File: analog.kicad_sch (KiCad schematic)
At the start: 38 parts, among them Q3 BSS138, U1 TL494, U4 NE5532, U5 INA180A2

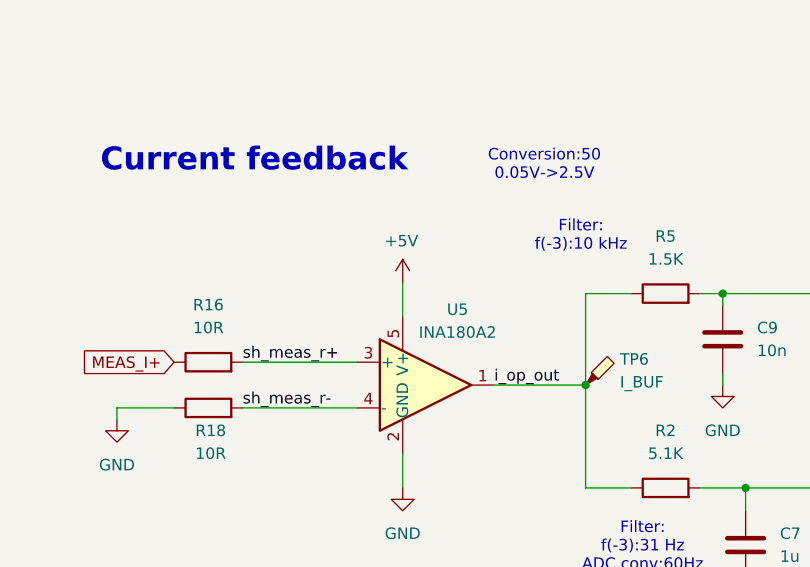
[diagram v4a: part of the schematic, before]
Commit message: approximate location of the components at the PCB
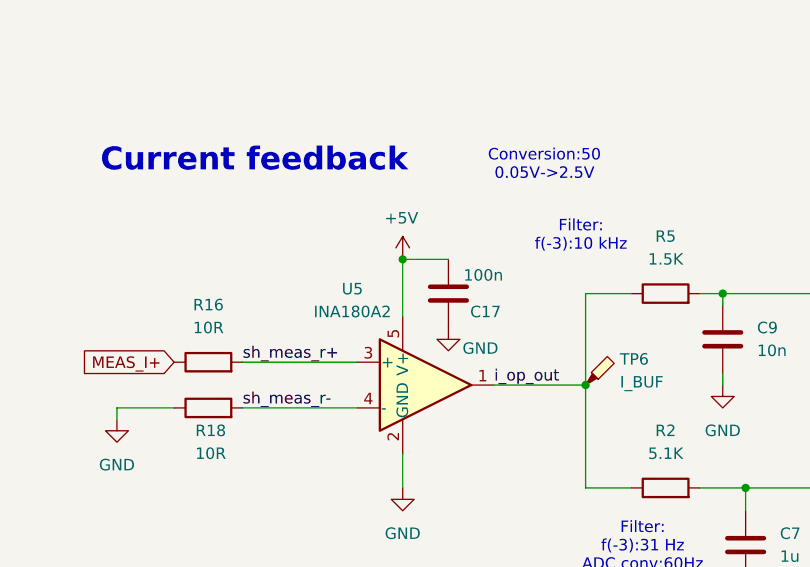
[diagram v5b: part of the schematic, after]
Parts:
- added C17: 100n, Capacitor_SMD:C_0805_2012Metric_Pad1.18x1.45mm_HandSolder, symbol Device:C
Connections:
- net +5V: now also C17.2
- net GND: now also C17.1
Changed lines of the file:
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@@
 	)
 	(junction
+		(at 62.23 133.35)
+		(diameter 0)
+		(color 0 0 0 0)
+	)
+	(junction
 		(at 250.19 97.79)
 		(diameter 0)
@@
 	(wire
 		(pts
+			(xy 62.23 133.35) (xy 67.31 133.35)
+		)
+		(stroke
+			(width 0)
+			(type default)
+		)
+	)
+	(wire
+		(pts
 			(xy 256.54 97.79) (xy 259.08 97.79)
 		)
@@
 	(wire
 		(pts
+			(xy 62.23 133.35) (xy 62.23 139.7)
+		)
+		(stroke
+			(width 0)
+			(type default)
+		)
+	)
+	(wire
+		(pts
 			(xy 107.95 38.1) (xy 105.41 38.1)
 		)
@@
 	(wire
 		(pts
-			(xy 62.23 135.89) (xy 62.23 139.7)
-		)
-		(stroke
-			(width 0)
-			(type default)
-		)
-	)
-	(wire
-		(pts
 			(xy 250.19 97.79) (xy 250.19 102.87)
 		)
@@
 	(symbol
 		(lib_id "power:GND")
+		(at 67.31 140.97 0)
+		(unit 1)
+		(exclude_from_sim no)
+		(in_bom yes)
+		(on_board yes)
+		(dnp no)
+		(property "Reference" "#PWR051"
+			(at 67.31 147.32 0)
+			(effects
+				(font
+					(size 1.27 1.27)
+				)
+				(hide yes)
+			)
+		)
+		(property "Value" "GND"
+			(at 70.866 143.256 0)
+			(effects
+				(font
+					(size 1.27 1.27)
+				)
+			)
+		)
+		(property "Footprint" ""
+			(at 67.31 140.97 0)
+			(effects
+				(font
+					(size 1.27 1.27)
+				)
+				(hide yes)
+			)
+		)
+		(property "Datasheet" ""
+			(at 67.31 140.97 0)
+			(effects
+				(font
+					(size 1.27 1.27)
+				)
+				(hide yes)
+			)
+		)
+		(property "Description" "Power symbol creates a global label with name \"GND\" , ground"
+			(at 67.31 140.97 0)
+			(effects
+				(font
+					(size 1.27 1.27)
+				)
+				(hide yes)
+			)
+		)
+		(pin "1"
+		)
+		(instances
+			(project "RPS_ATX"
+				(path "/485c2fed-5176-4ba8-b79d-ac7eddb44491/75639b50-c04a-47dd-b6e6-c8da699a633c"
+					(reference "#PWR051")
+					(unit 1)
+				)
+			)
+		)
+	)
+	(symbol
+		(lib_id "power:GND")
 		(at 92.71 35.56 0)
 		(unit 1)
@@
 		(dnp no)
 		(property "Reference" "U5"
-			(at 68.326 138.938 0)
+			(at 56.642 136.652 0)
 			(effects
 				(font
@@
 		)
 		(property "Value" "INA180A2"
-			(at 68.326 141.478 0)
+			(at 56.642 139.192 0)
 			(effects
 				(font
@@
 	(symbol
 		(lib_id "power:+2V5")
-		(at 62.23 135.89 0)
+		(at 62.23 133.35 0)
 		(unit 1)
 		(exclude_from_sim no)
@@
 		(dnp no)
 		(property "Reference" "#PWR01"
-			(at 62.23 139.7 0)
+			(at 62.23 137.16 0)
 			(effects
 				(font
@@
 		)
 		(property "Value" "+5V"
-			(at 60.198 131.318 0)
+			(at 60.198 128.778 0)
 			(effects
 				(font
@@
 		)
 		(property "Footprint" ""
-			(at 62.23 135.89 0)
+			(at 62.23 133.35 0)
 			(effects
 				(font
@@
 		)
 		(property "Datasheet" ""
-			(at 62.23 135.89 0)
+			(at 62.23 133.35 0)
 			(effects
 				(font
@@
 		)
 		(property "Description" "Power symbol creates a global label with name \"+2V5\""
-			(at 62.23 135.89 0)
+			(at 62.23 133.35 0)
 			(effects
 				(font
@@
 					(unit 1)
 				)
+			)
+		)
+	)
+	(symbol
+		(lib_id "Device:C")
+		(at 67.31 137.16 180)
+		(unit 1)
+		(exclude_from_sim no)
+		(in_bom yes)
+		(on_board yes)
+		(dnp no)
+		(property "Reference" "C17"
+			(at 73.152 139.192 0)
+			(effects
+				(font
+					(size 1.27 1.27)
+				)
+				(justify left)
+			)
+		)
+		(property "Value" "100n"
+			(at 73.406 135.128 0)
+			(effects
+				(font
+					(size 1.27 1.27)
+				)
+				(justify left)
+			)
+		)
+		(property "Footprint" "Capacitor_SMD:C_0805_2012Metric_Pad1.18x1.45mm_HandSolder"
+			(at 66.3448 133.35 0)
+			(effects
+				(font
+					(size 1.27 1.27)
+				)
+				(hide yes)
+			)
+		)
+		(property "Datasheet" "~"
+			(at 67.31 137.16 0)
+			(effects
+				(font
+					(size 1.27 1.27)
+				)
+				(hide yes)
+			)
+		)
+		(property "Description" "Unpolarized capacitor"
+			(at 67.31 137.16 0)
+			(effects
+				(font
+					(size 1.27 1.27)
+				)
+				(hide yes)
+			)
+		)
+		(pin "2"
+		)
+		(pin "1"
+		)
+		(instances
+			(project "RPS_ATX"
+				(path "/485c2fed-5176-4ba8-b79d-ac7eddb44491/75639b50-c04a-47dd-b6e6-c8da699a633c"
+					(reference "C17")
+					(unit 1)
+				)

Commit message: final location of the power,analog sections
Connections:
- net I_2IN-: now also R25.2; no longer C9.1, R5.2
- net U_1IN-: now also R24.2; no longer C18.1, R14.2
- net I_2IN+: now reaches U1.16 (2IN+)
- net I_2IN+: now also C9.1, R5.2; no longer R25.2
- net U_1IN+: now reaches U1.1 (1IN+)
- net U_1IN+: now also C18.1, R14.2; no longer R24.2
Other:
- moved on the sheet: C19, C3, C34, C35, C4, C5, Q3, R1, R13, R24, R25, R3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

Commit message: added display and encoders signal lines, hints
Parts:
- removed U4: NE5532, Package_SO:SOIC-8_3.9x4.9mm_P1.27mm, symbol Amplifier_Operational:NE5532
- added C13, C14: 100n, Capacitor_SMD:C_0805_2012Metric_Pad1.18x1.45mm_HandSolder, symbol Device:C
- added U9: OP07, Package_SO:SOIC-8_3.9x4.9mm_P1.27mm, symbol Amplifier_Operational:OP07
- RV1: value 100K -> U_RV
- RV2: value 100K -> I_RV
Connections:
- net +15V: now also C14.1, U9.7 (V+)
- net GND: now also C13.2, C14.2
- net at R14.1, R15.2, R17.1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: now also U9.6
- net at R15.1, R6.2: now also U9.2 (-)
- net at R4.2, R8.1: now also U9.3 (+)
- new net -5V: C13.1, U9.4 (V-)
- no-connect marks 0 -> 2
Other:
- moved on the sheet: R15, R8

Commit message: added fan control and ds18b20 to the schematic
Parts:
- removed Q3: BSS138, Package_TO_SOT_SMD:SOT-23, symbol Transistor_FET:BSS138
- added Q2: AO3400A, Package_TO_SOT_SMD:SOT-23, symbol Transistor_FET:AO3400A
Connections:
- net DTC: now also Q2.3 (D)
- net GND: now also Q2.2 (S)
- net at C5.1, R1.2: now also Q2.1 (G)
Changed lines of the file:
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@@
+	)
+	(symbol
+		(lib_id "Transistor_FET:AO3400A")
+		(at 250.19 142.24 0)
+		(unit 1)
+		(exclude_from_sim no)
+		(in_bom yes)
+		(on_board yes)
+		(dnp no)
+		(fields_autoplaced yes)
+		(property "Reference" "Q2"
+			(at 256.54 140.9699 0)
+			(effects
+				(font
+					(size 1.27 1.27)
+				)
+				(justify left)
+			)
+		)
+		(property "Value" "AO3400A"
+			(at 256.54 143.5099 0)
+			(effects
+				(font
+					(size 1.27 1.27)
+				)
+				(justify left)
+			)
+		)
+		(property "Footprint" "Package_TO_SOT_SMD:SOT-23"
+			(at 255.27 144.145 0)
+			(effects
+				(font
+					(size 1.27 1.27)
+					(italic yes)
+				)
+				(justify left)
+				(hide yes)
+			)
+		)
+		(property "Datasheet" "http://www.aosmd.com/pdfs/datasheet/AO3400A.pdf"
+			(at 255.27 146.05 0)
+			(effects
+				(font
+					(size 1.27 1.27)
+				)
+				(justify left)
+				(hide yes)
+			)
+		)
+		(property "Description" "30V Vds, 5.7A Id, N-Channel MOSFET, SOT-23"
+			(at 250.19 142.24 0)
+			(effects
+				(font
+					(size 1.27 1.27)
+				)
+				(hide yes)
+			)
+		)
+		(pin "3"
+		)
+		(pin "2"
+		)
+		(pin "1"
+		)
+		(instances
+			(project "RPS_ATX"
+				(path "/485c2fed-5176-4ba8-b79d-ac7eddb44491/75639b50-c04a-47dd-b6e6-c8da699a633c"
+					(reference "Q2")
+					(unit 1)
+				)
+			)
+		)
 	)
 	(symbol
@@
 					(unit 1)
 				)
-			)
-		)
-	)
-	(symbol
-		(lib_id "Transistor_FET:BSS138")
-		(at 250.19 142.24 0)
-		(unit 1)
-		(exclude_from_sim no)
-		(in_bom yes)
-		(on_board yes)
-		(dnp no)
-		(fields_autoplaced yes)
-		(property "Reference" "Q3"
-			(at 256.54 140.9699 0)
-			(effects
-				(font
-					(size 1.27 1.27)
-				)
-				(justify left)
-			)
-		)
-		(property "Value" "BSS138"
-			(at 256.54 143.5099 0)
-			(effects
-				(font
-					(size 1.27 1.27)
-				)
-				(justify left)
-			)
-		)
-		(property "Footprint" "Package_TO_SOT_SMD:SOT-23"
-			(at 255.27 144.145 0)
-			(effects
-				(font
-					(size 1.27 1.27)
-					(italic yes)
-				)
-				(justify left)
-				(hide yes)
-			)
-		)
-		(property "Datasheet" "https://www.onsemi.com/pub/Collateral/BSS138-D.PDF"
-			(at 255.27 146.05 0)
-			(effects
-				(font
-					(size 1.27 1.27)
-				)
-				(justify left)
-				(hide yes)
-			)
-		)
-		(property "Description" "50V Vds, 0.22A Id, N-Channel MOSFET, SOT-23"
-			(at 250.19 142.24 0)
-			(effects
-				(font
-					(size 1.27 1.27)
-				)
-				(hide yes)
-			)
-		)
-		(pin "2"
-		)
-		(pin "3"
-		)
-		(pin "1"
-		)
-		(instances
-			(project "RPS_ATX"
-				(path "/485c2fed-5176-4ba8-b79d-ac7eddb44491/75639b50-c04a-47dd-b6e6-c8da699a633c"
-					(reference "Q3")
-					(unit 1)
-				)
